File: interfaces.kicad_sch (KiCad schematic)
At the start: 87 parts, among them IC3 TPD8S009DSMR, J4 WE_629105150521, J6 685119134923, J7 1140084168, Q2 BSS138APW, Q3 BSS138APW, Q4 BSS138APW, Q5 BSS138APW, Q6 BSS138APW, U7 FT4232HQ, Y2 ABM8G-12.000MHZ-18-D2Y-T

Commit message: Loclib
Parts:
- U7: footprint antmicro-footprints:FT4232HQ -> data-center-dram-tester-footprints:FT4232HQ; symbol antmicroInterfaceControllers:FT4232HQ -> data-center-dram-tester:FT4232HQ
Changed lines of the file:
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@@
     (pin "2")
   )
-  (symbol (lib_id "antmicroInterfaceControllers:FT4232HQ") (at 100.965 105.41 0) (unit 1)
+  (symbol (lib_id "data-center-dram-tester:FT4232HQ") (at 100.965 105.41 0) (unit 1)
     (in_bom yes) (on_board yes)
     (property "Reference" "U7" (id 0) (at 100.965 42.2402 0)
@@
       (effects (font (size 1.524 1.524)))
     )
-    (property "Footprint" "antmicro-footprints:FT4232HQ" (id 2) (at 106.045 100.33 90)
+    (property "Footprint" "data-center-dram-tester-footprints:FT4232HQ" (id 2) (at 106.045 100.33 90)
       (effects (font (size 1.524 1.524)) (justify left) hide)
     )

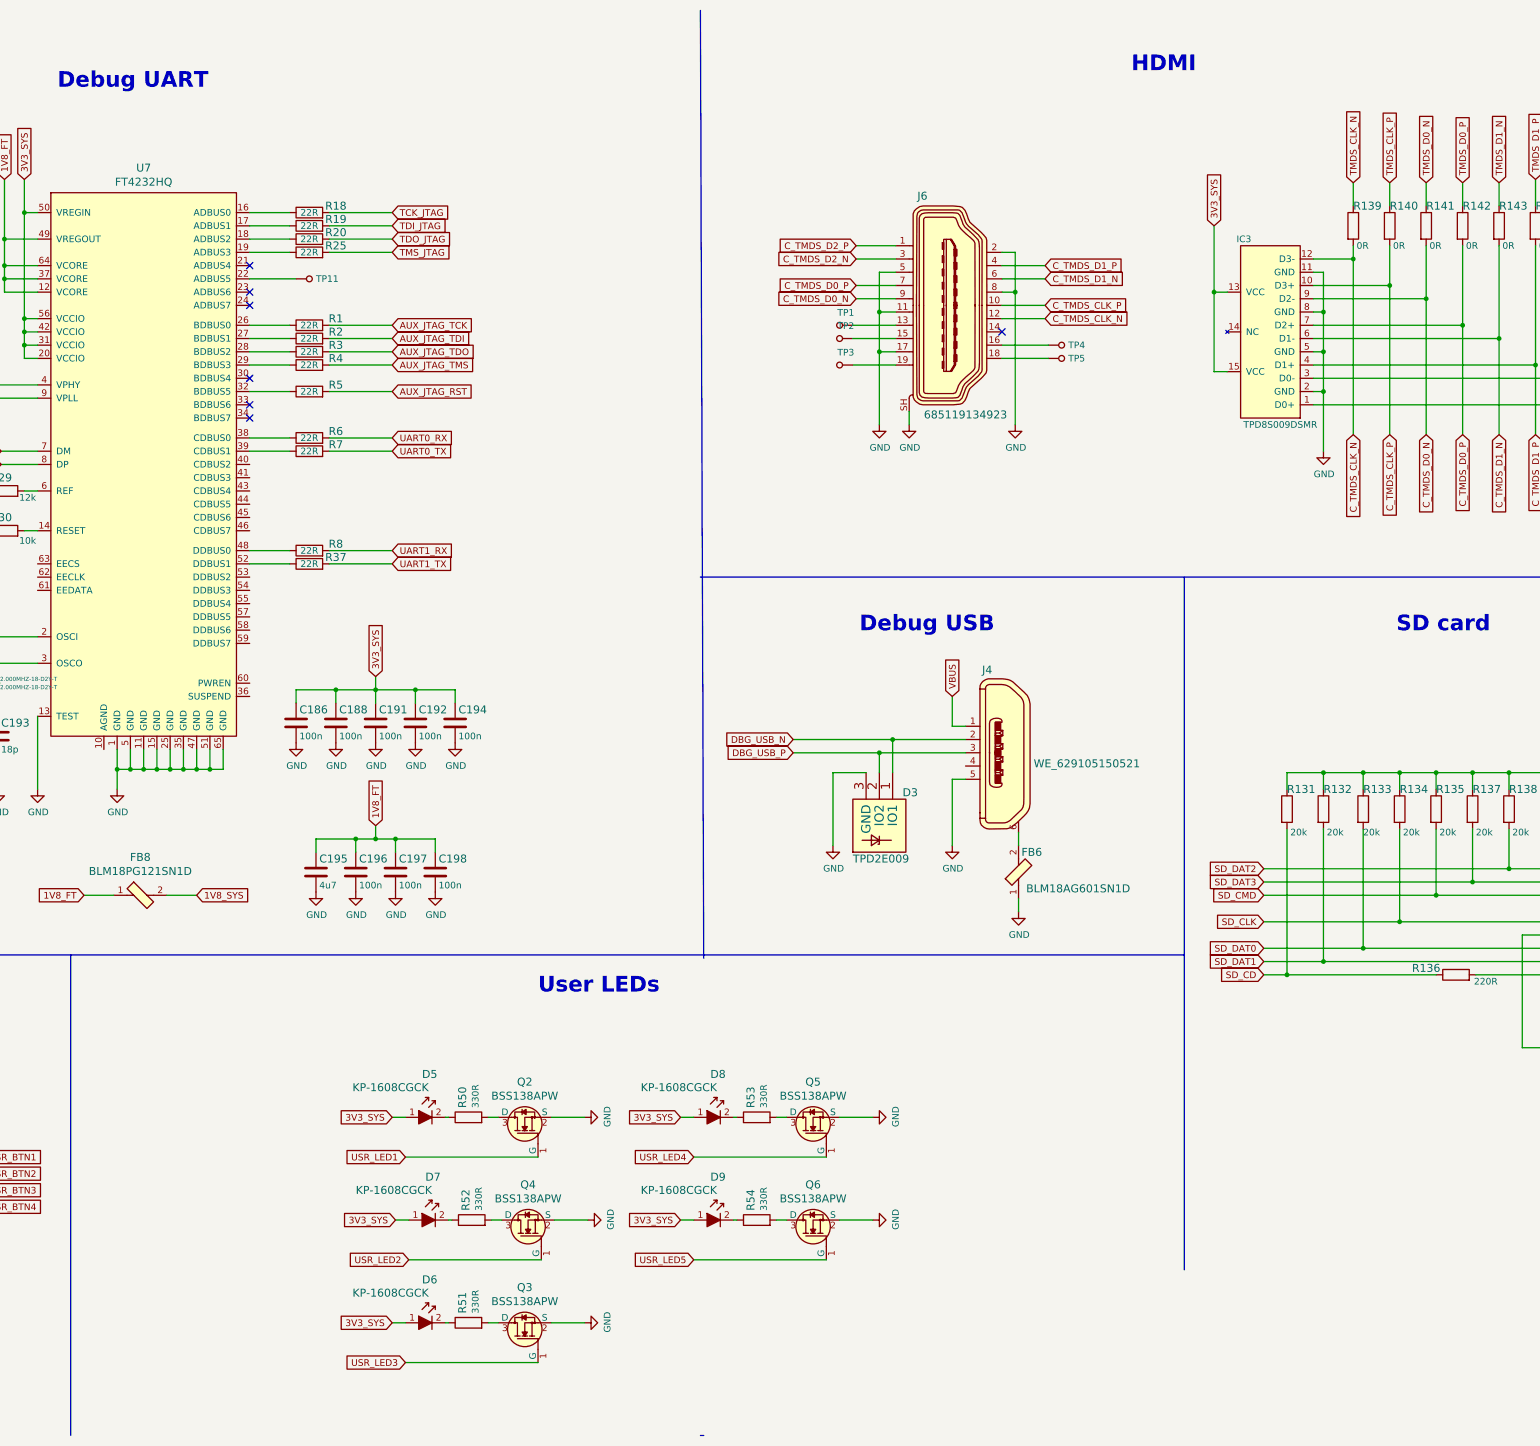
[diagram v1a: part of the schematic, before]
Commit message: Added hot-swap: button, LED indication, detection on ground pin. Updated SN74LVC1G07 symbol
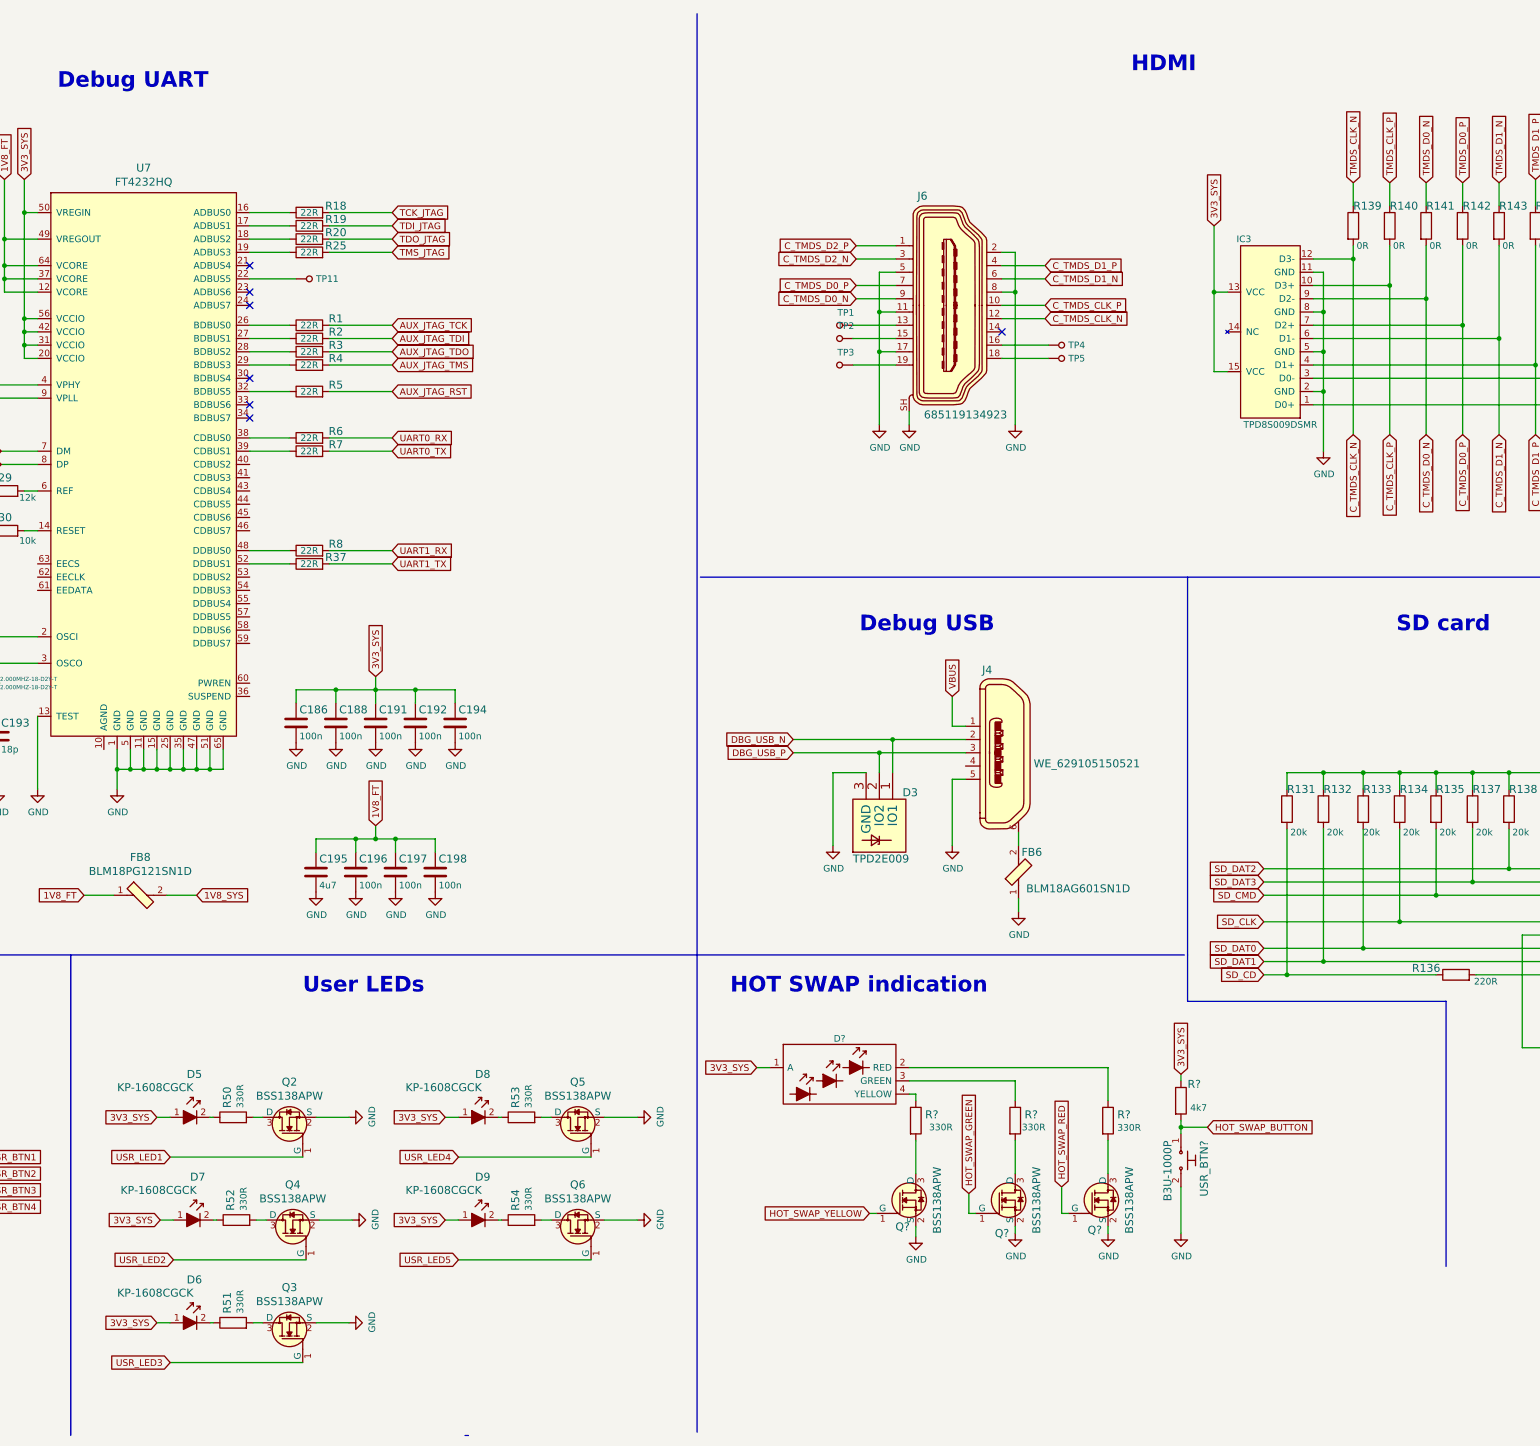
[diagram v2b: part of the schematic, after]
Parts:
- added D?: APTF1616SURKCGKSYKC, antmicro-footprints:KPTF1616RGBC11, symbol antmicroLEDIndicationDiscrete:APTF1616SURKCGKSYKC
- added Q? (x3): BSS138APW, data-center-dram-tester-footprints:SC70-3, symbol data-center-dram-tester:BSS138APW
- added R?: R_4k7_0402, data-center-dram-tester-footprints:0402-res, symbol data-center-dram-tester:R_4k7_0402
- added R? (x3): R_330R_0402, data-center-dram-tester-footprints:0402-res, symbol data-center-dram-tester:R_330R_0402
- added USR_BTN?: B3U-1000P, data-center-dram-tester-footprints:Switch_Tactile_SMD_B3U-1000P, symbol data-center-dram-tester:B3U-1000P
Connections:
- net 3V3_SYS: now also D?.1 (A), R?.1
- net GND: now also Q?.2 (S), Q?.2 (S), Q?.2 (S), USR_BTN?.2
- new net: Q?.3 (D), R?.2 (x3)
- new net: D?.4 (YELLOW), R?.1
- new net: D?.2 (RED), R?.1
- new net: D?.3 (GREEN), R?.1
- new net HOT_SWAP_BUTTON: R?.2, USR_BTN?.1
- new net HOT_SWAP_GREEN: Q?.1 (G)
- new net HOT_SWAP_RED: Q?.1 (G)
- new net HOT_SWAP_YELLOW: Q?.1 (G)
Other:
- note added: "HOT SWAP indication"
- moved on the sheet: D5, D6, D7, D8, D9, Q2, Q3, Q4, Q5, Q6, R50, R51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
